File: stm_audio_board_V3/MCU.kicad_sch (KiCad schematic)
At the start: 14 parts, among them SW1 SW_SPST, U7 STM32H723ZGTx, Y2 X1E0000210132

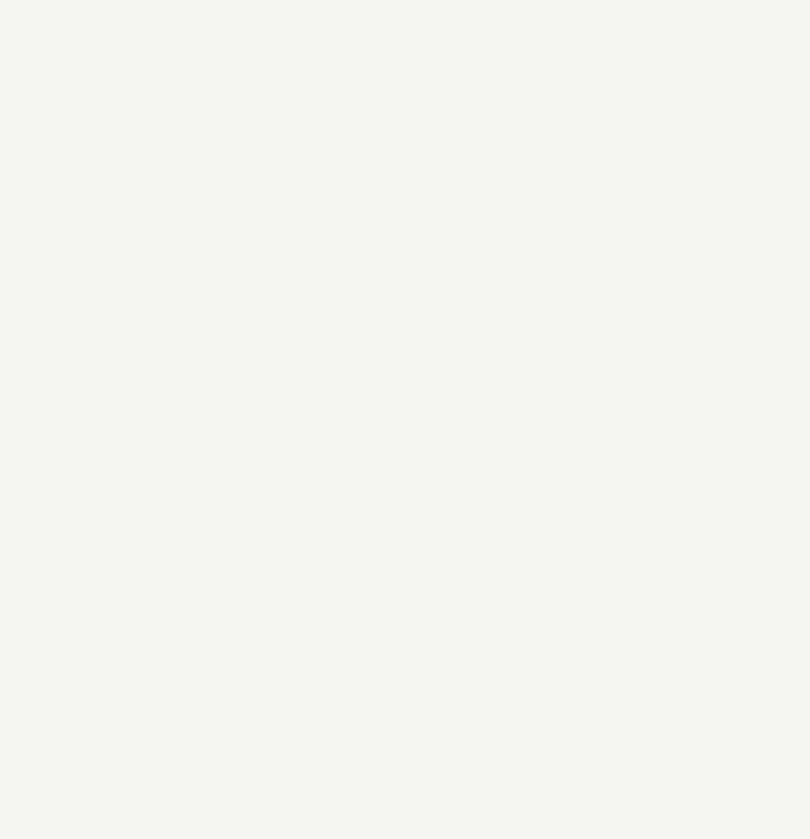
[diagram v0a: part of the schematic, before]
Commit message: SDRAM symbol added
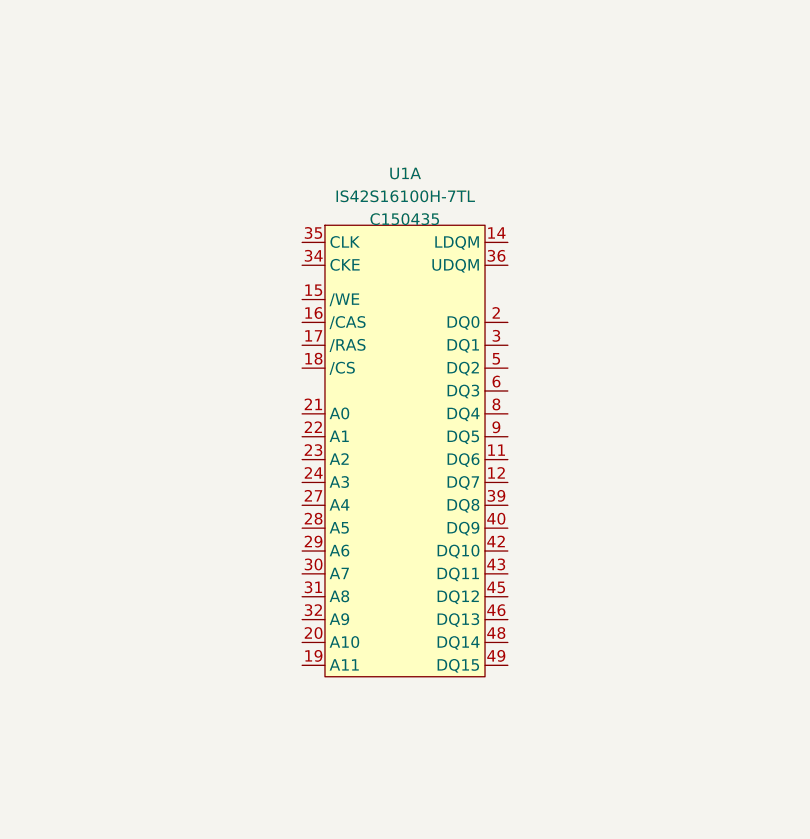
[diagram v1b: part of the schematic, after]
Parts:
- added U1: IS42S16100H-7TL, Package_SO:TSSOP-50_4.4x12.5mm_P0.5mm, symbol stm_audio:IS42S16100H-7TL

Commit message: pcb redesign
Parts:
- U1: footprint Package_SO:TSSOP-50_4.4x12.5mm_P0.5mm -> Library:TSOP-2-50-new

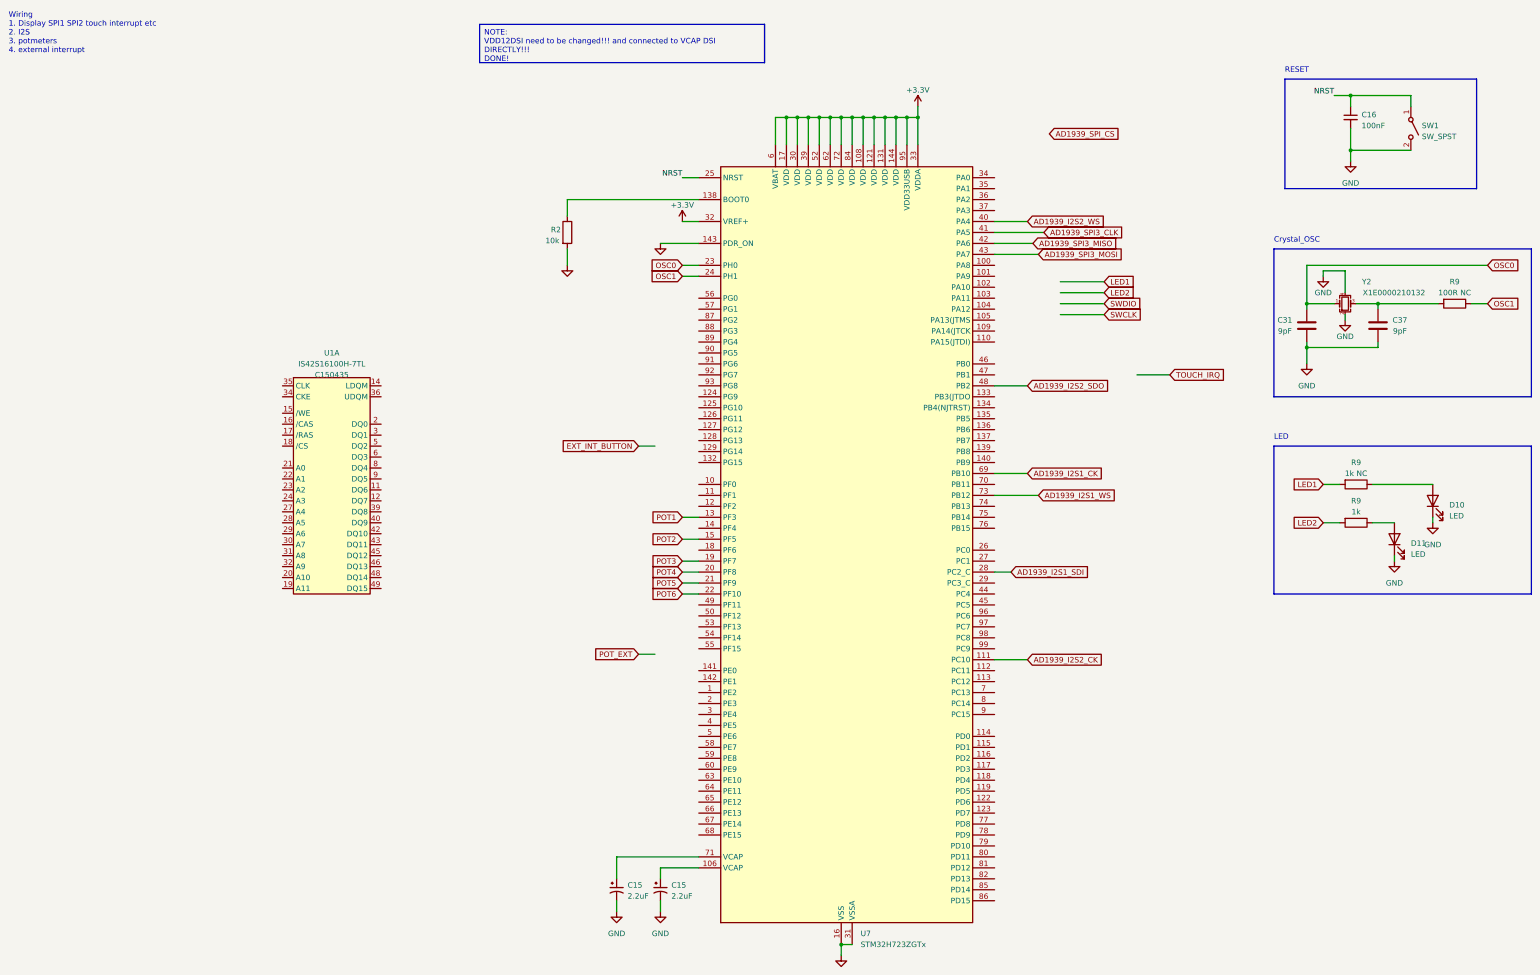
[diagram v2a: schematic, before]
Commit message: Input and output stages are made and assembly started on pcb view
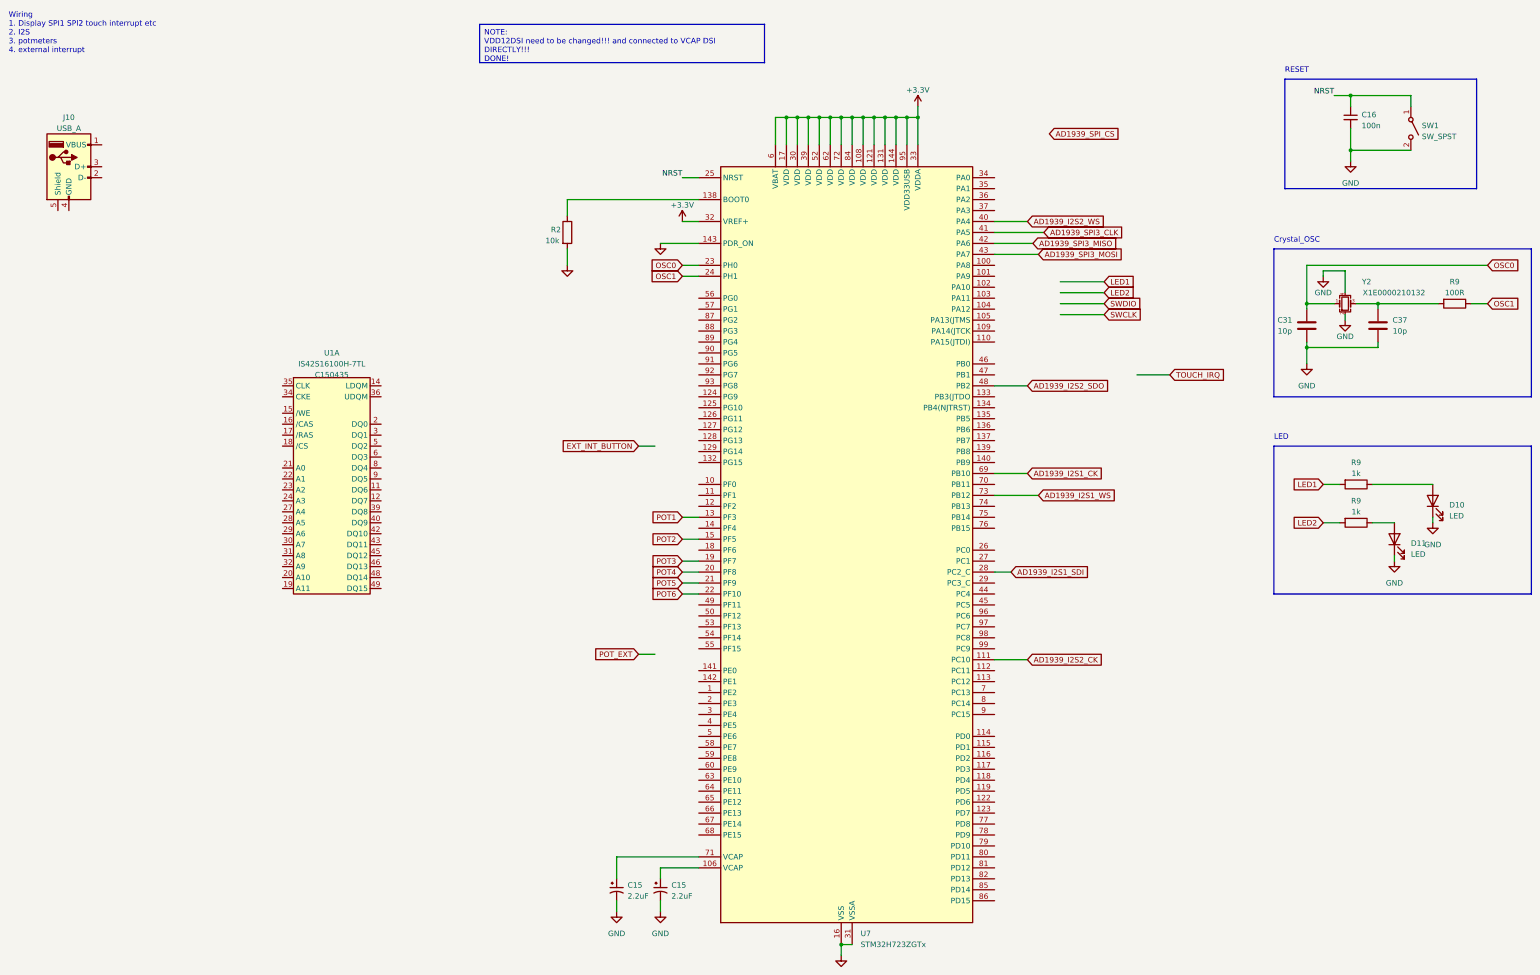
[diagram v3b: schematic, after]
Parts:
- added J10: USB_A, Connector_USB:USB_A_CONNFLY_DS1095-WNR0, symbol Connector:USB_A
- C16: value 100nF -> 100n; footprint Capacitor_SMD:C_0603_1608Metric_Pad1.08x0.95mm_HandSolder -> Capacitor_SMD:C_0603_1608Metric
- C31, C37: value 9pF -> 10p; footprint Capacitor_SMD:C_0603_1608Metric_Pad1.08x0.95mm_HandSolder -> Capacitor_SMD:C_0603_1608Metric
- R2: footprint Resistor_SMD:R_0805_2012Metric_Pad1.20x1.40mm_HandSolder -> Resistor_SMD:R_0603_1608Metric
- R9: value 100R NC -> 100R; footprint Resistor_SMD:R_0603_1608Metric_Pad0.98x0.95mm_HandSolder -> Resistor_SMD:R_0603_1608Metric
- R9: value 1k NC -> 1k

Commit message: Input output connected to codec
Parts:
- U7: JLCPCB (none) -> C730146
